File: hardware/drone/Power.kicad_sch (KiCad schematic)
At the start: 100 parts, among them Q1 ISP650P06NM, U1 STM32N645I0, U12 LP5907, U16 LMR51635XFDDCR, U18 TPS2121, U3 TPS628303, U4 TPS7A2118PQWDSGRQ1, U5 TPS628303

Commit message: Started layout and tested RF routing paths
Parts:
- U1: footprint (none) -> STM32N645I0:BGA178C80P14X14_1200X1200X100
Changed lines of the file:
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@@
 			)
 		)
-		(property "Footprint" ""
+		(property "Footprint" "STM32N645I0:BGA178C80P14X14_1200X1200X100"
 			(at 252.73 149.86 0)
 			(hide yes)
@@
 			)
 		)
-		(property "Footprint" ""
+		(property "Footprint" "STM32N645I0:BGA178C80P14X14_1200X1200X100"
 			(at 346.71 120.65 0)
 			(hide yes)

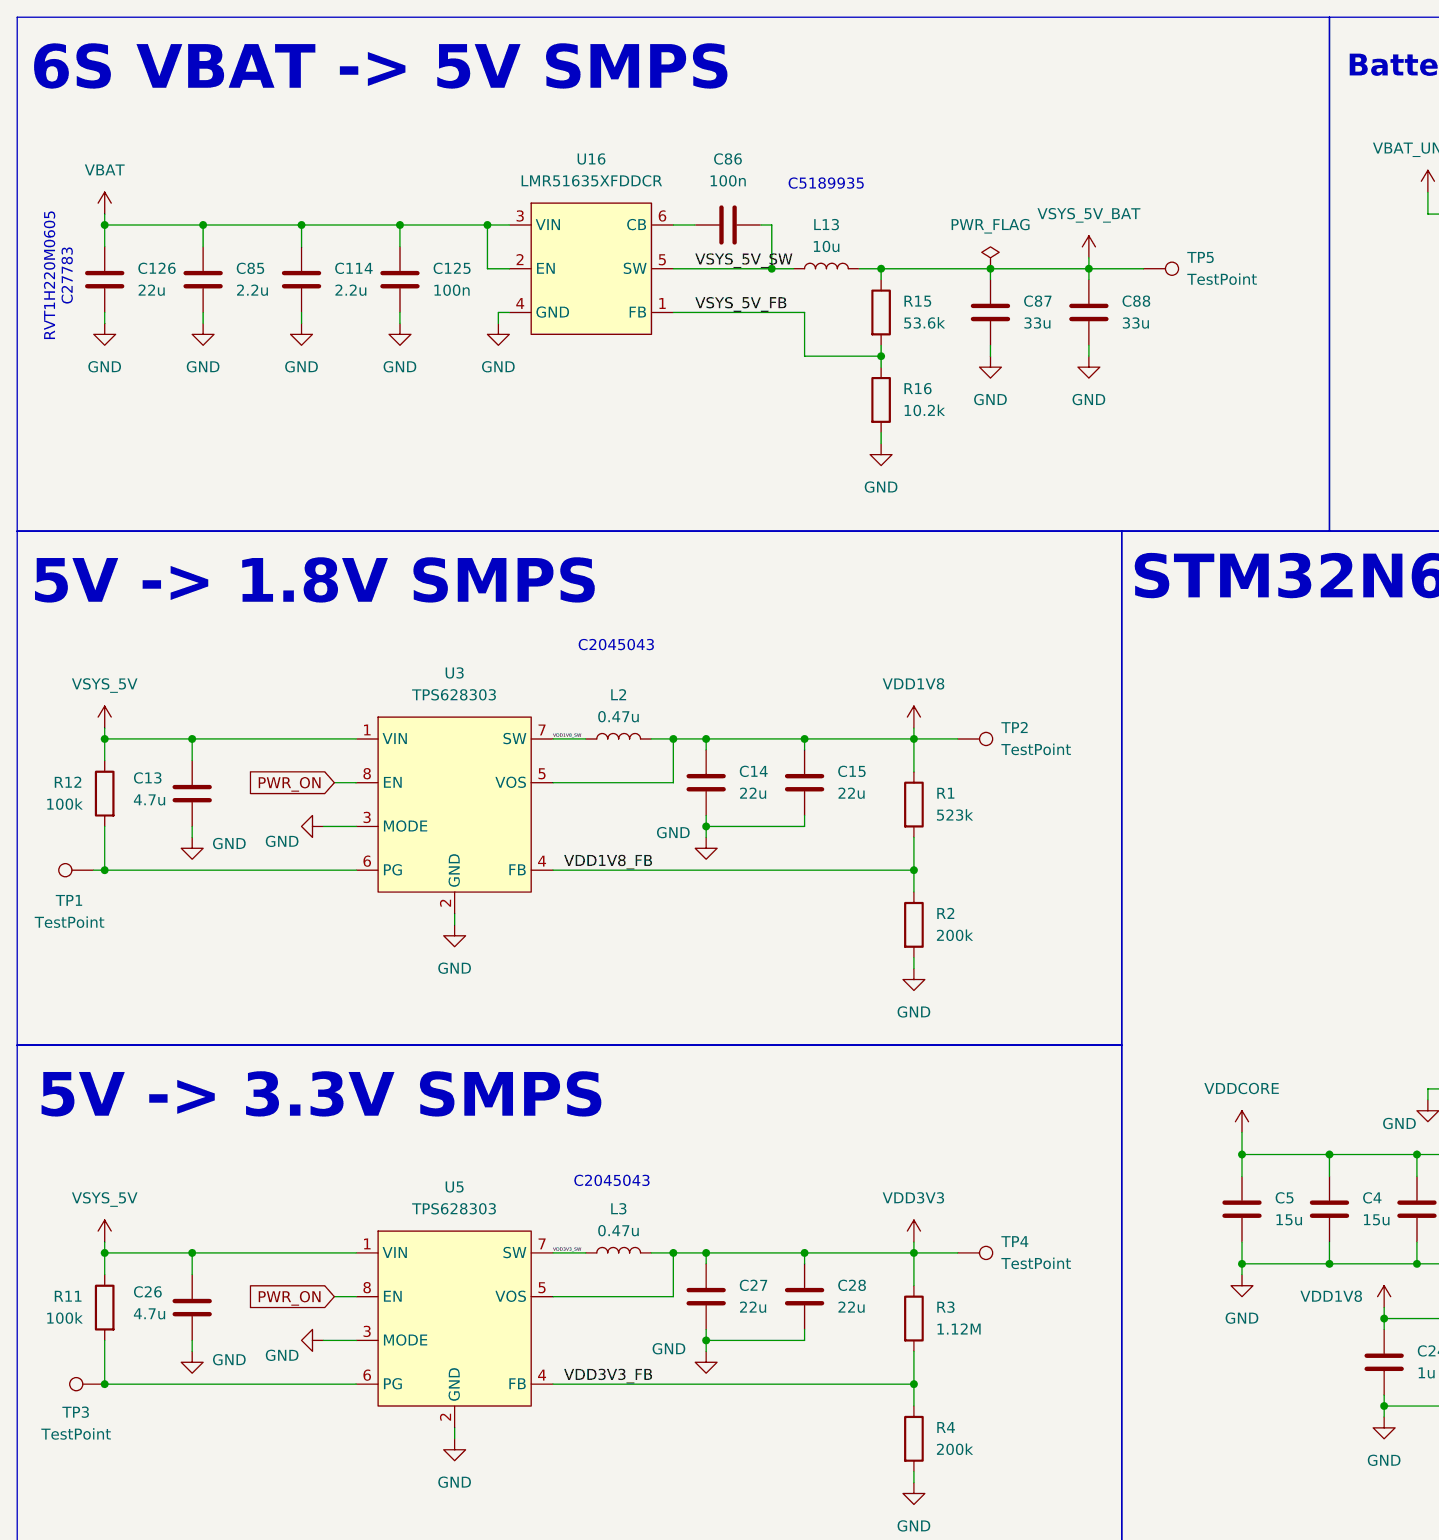
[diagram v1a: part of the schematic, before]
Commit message: Placed SMPS layouts and optimized for space
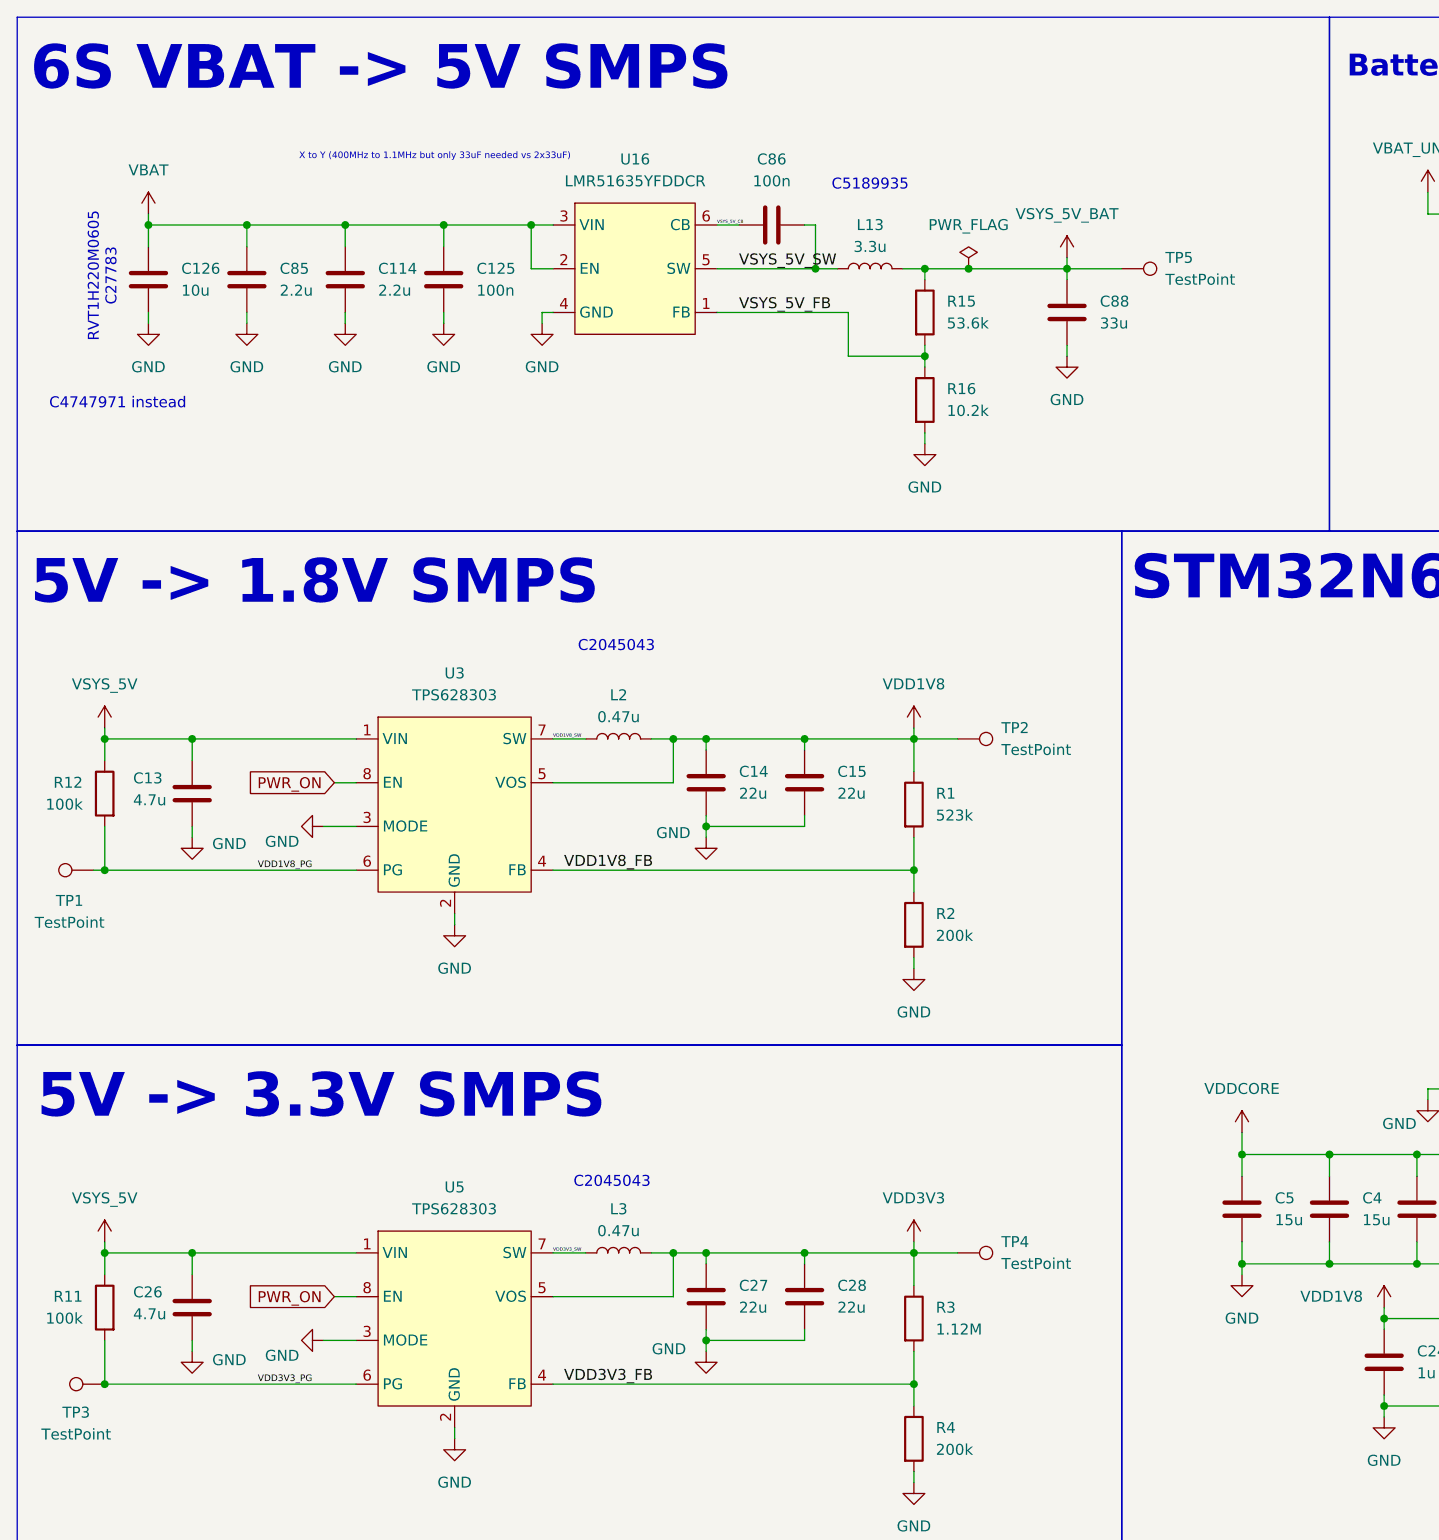
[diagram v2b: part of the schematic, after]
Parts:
- removed C87: 33u, Capacitor_SMD:C_1812_4532Metric, symbol Device:C
- C126: value 22u -> 10u; footprint Capacitor_SMD:CP_Elec_6.3x5.4 -> Capacitor_SMD:CP_Elec_5x5.4
- L13: value 10u -> 3.3u; footprint SoftDroneLibrary:CYA0650-10UH -> SoftDroneLibrary:74439324033
- U16: value LMR51635XFDDCR -> LMR51635YFDDCR
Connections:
- net VSYS_5V_CB: now reaches C86.1, U16.6 (CB)
- net VDD3V3_PG: now reaches R11.2, TP3.1, U5.6 (PG)
- net VDD1V8_PG: now reaches R12.2, TP1.1, U3.6 (PG)
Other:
- note added: "C4747971 instead"
- note added: "X to Y (400MHz to 1.1MHz but only 33uF needed vs 2x33uF)"
- moved on the sheet: C114, C125, C126, C85, C86, C88, L13, R15, R16, TP5, U16

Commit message: Routed OSPI
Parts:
- removed C126: 10u, Capacitor_SMD:CP_Elec_5x5.4, symbol Device:C
- removed Q1: ISP650P06NM, Package_TO_SOT_SMD:SOT-223, symbol Simulation_SPICE:PMOS
- added U13: SQA411CEJW-T1_GE3, SQA411CEJW-T1_GE3:SQA411CEJWT1_GE3, symbol SoftDrone:SQA411CEJW-T1_GE3
- F1: value 2920L150/60MR -> SF-0603SP200R-2; footprint Fuse:Fuse_2920_7451Metric -> Fuse:Fuse_0603_1608Metric
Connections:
- net VBAT: now also U13.4 (S), U13.7 (S)
- net VBAT_PMOS_D: now also U13.1 (D), U13.2 (D), U13.5 (D), U13.6 (D), U13.8 (D)
- net VBAT_PMOS_G: now also U13.3 (G)
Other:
- note added: "C4747971 instead (if bulk 10u cap is placed)"
- note removed: "C4747971 instead"
- moved on the sheet: D1, D2, F1, R24

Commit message: Placed connectors and bucks
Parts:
- D2: value SMBJ30CA -> 6DFN36CA; footprint Diode_SMD:D_SMB -> SoftDroneLibrary:6DFN12CA
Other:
- note added: "C24668140"
- note removed: "C5189935"
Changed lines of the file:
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@@
 		)
 	)
-	(text "C5189935"
+	(text "C24668140"
 		(exclude_from_sim no)
-		(at 132.08 56.388 0)
+		(at 132.334 57.658 0)
 		(effects
 			(font
-				(size 1.27 1.27)
+				(size 1.016 1.016)
 			)
 		)
@@
 			)
 		)
-		(property "Value" "SMBJ30CA"
+		(property "Value" "6DFN36CA"
 			(at 208.28 63.5 90)
 			(show_name no)
@@
 			)
 		)
-		(property "Footprint" "Diode_SMD:D_SMB"
+		(property "Footprint" "SoftDroneLibrary:6DFN12CA"
 			(at 205.74 62.23 0)
 			(hide yes)

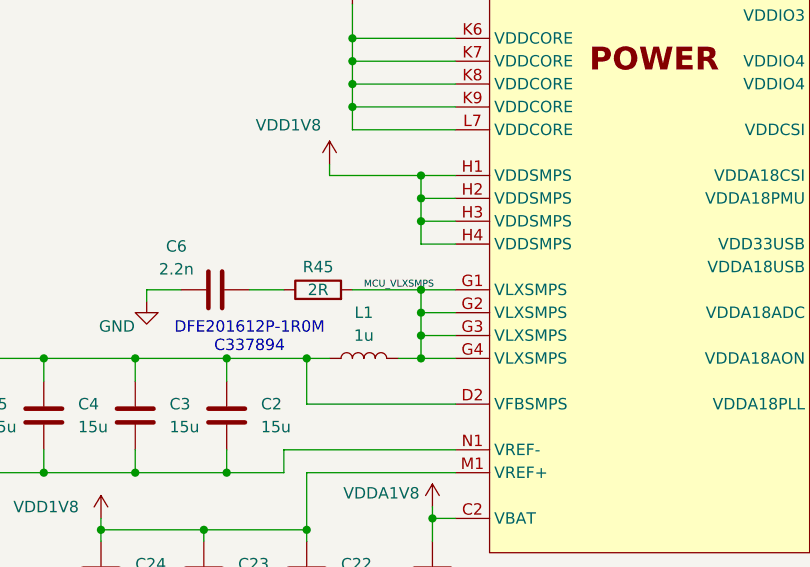
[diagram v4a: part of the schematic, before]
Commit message: MCU decap placement and camera connector placement
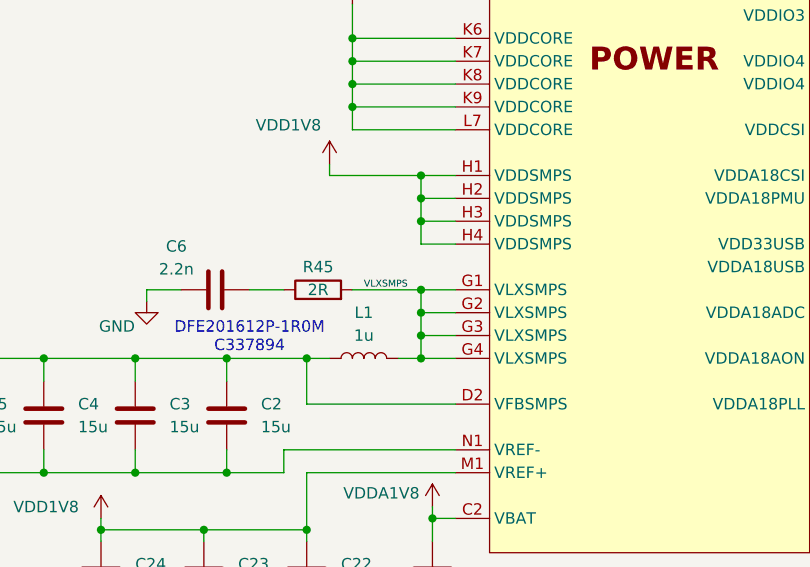
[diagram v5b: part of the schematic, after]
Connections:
- net MCU_VLXSMPS renamed VLXSMPS
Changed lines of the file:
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@@
 		)
 	)
-	(label "MCU_VLXSMPS"
+	(label "VLXSMPS"
 		(at 220.98 161.29 0)
 		(effects

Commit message: More power routing
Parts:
- added C128: 1u, Capacitor_SMD:C_0603_1608Metric, symbol Device:C
- added C129: 100n, Capacitor_SMD:C_0402_1005Metric, symbol Device:C
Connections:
- net GND: now also C128.2, C129.2
- net VSYS_5V_BAT: now also C128.1, C129.1

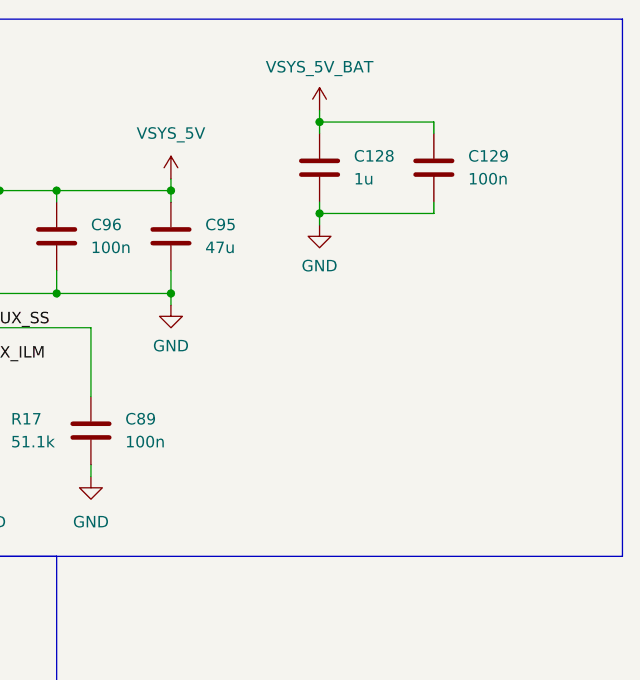
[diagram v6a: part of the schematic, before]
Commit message: Added power mux input decoupling
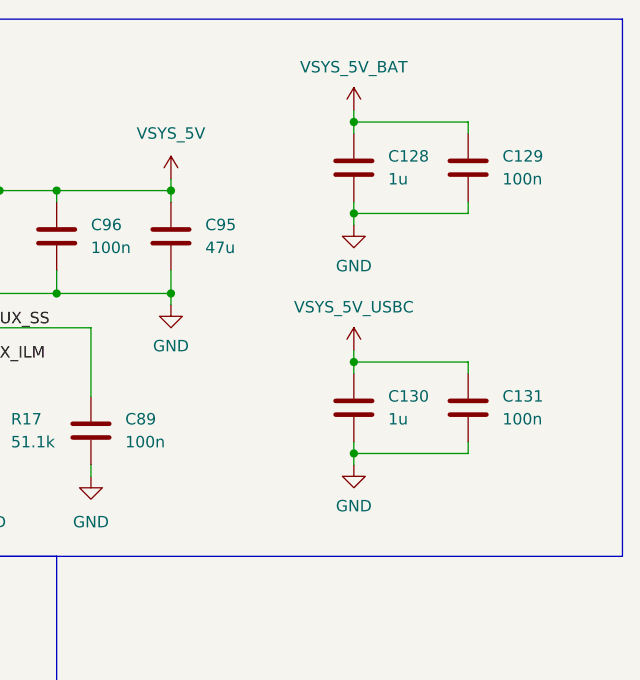
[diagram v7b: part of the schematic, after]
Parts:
- added C130: 1u, Capacitor_SMD:C_0603_1608Metric, symbol Device:C
- added C131: 100n, Capacitor_SMD:C_0402_1005Metric, symbol Device:C
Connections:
- net GND: now also C130.2, C131.2
- net VSYS_5V_USBC: now also C130.1, C131.1
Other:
- moved on the sheet: C128, C129

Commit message: Small cleanup and more power routing
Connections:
- net VSYS_5V_VBAT is gone; now on net VSYS_5V_BAT: R22.1
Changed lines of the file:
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@@
 			)
 		)
-		(property "Value" "VSYS_5V_VBAT"
+		(property "Value" "VSYS_5V_BAT"
 			(at 309.372 51.816 0)
 			(show_name no)
